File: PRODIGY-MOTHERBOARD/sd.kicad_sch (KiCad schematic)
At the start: 8 parts, among them J21 DM3BT-DSF-PEJS/C, Q1 DMP2045U-7, U4 IP4252CZ16

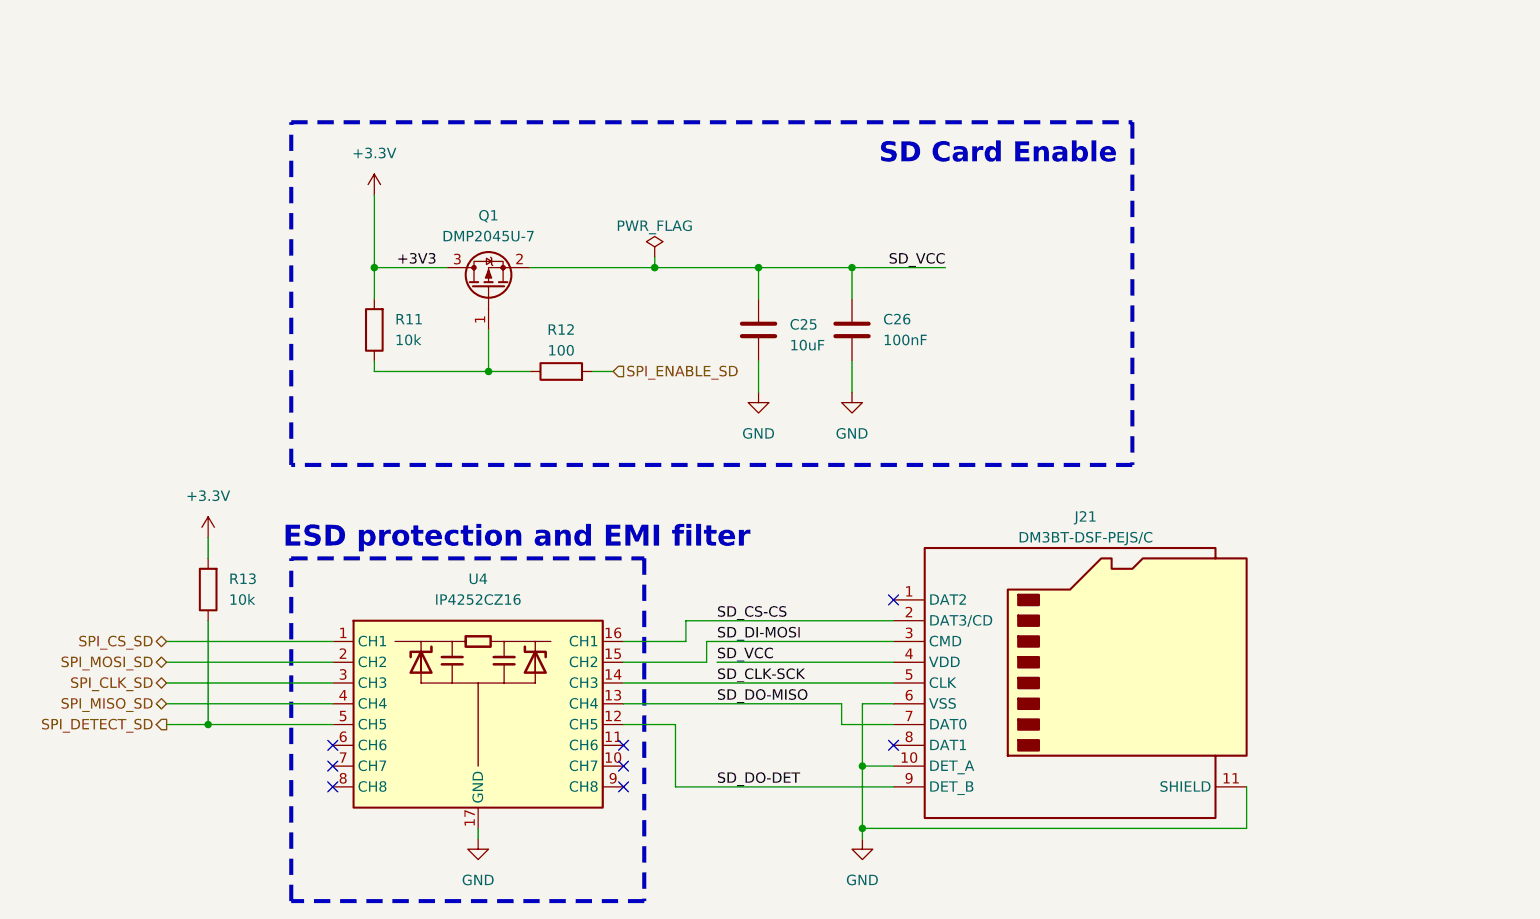
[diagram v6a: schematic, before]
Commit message: Submitted V0 for evaluation. Avaiting feedback.
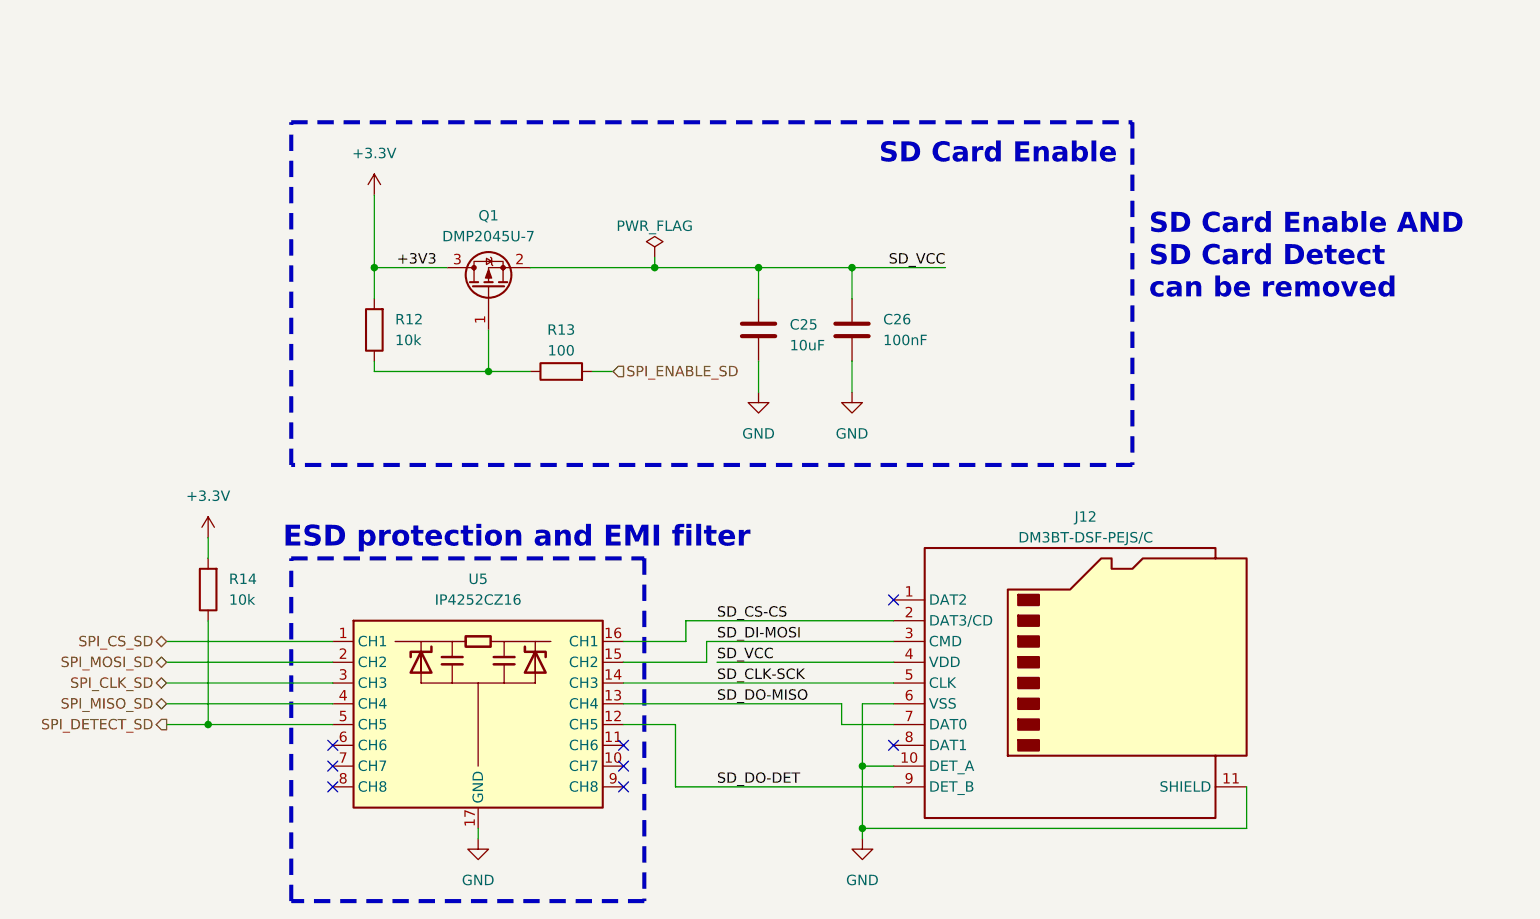
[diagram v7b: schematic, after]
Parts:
- renumbered J21 to J12, R11 to R12, R12 to R13, R13 to R14, U4 to U5
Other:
- note added: "SD Card Enable AND SD Card Detect can be removed"
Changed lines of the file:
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@@
 		)
 	)
-	(text "SD Card Enable"
-		(exclude_from_sim no)
-		(at 172.212 45.974 0)
+	(text "SD Card Enable AND\nSD Card Detect\ncan be removed"
+		(exclude_from_sim no)
+		(at 205.232 62.484 0)
 		(effects
 			(font
@@
 		)
 	)
+	(text "SD Card Enable"
+		(exclude_from_sim no)
+		(at 172.212 45.974 0)
+		(effects
+			(font
+				(size 2.45 2.45)
+				(thickness 0.49)
+				(bold yes)
+			)
+			(justify left bottom)
+		)
+	)
 	(label "SD_DI-MOSI"
 		(at 152.4 104.14 0)
@@
 		(dnp no)
 		(fields_autoplaced yes)
-		(property "Reference" "#PWR040"
+		(property "Reference" "#PWR064"
 			(at 123.19 134.62 0)
 			(effects
@@
 			(project "PRODIGY-MOTHERBOARD"
 				(path "/f1c25860-8989-4190-bd24-2491d23ca7d9/e2913798-f444-47a6-8b64-53020d7d816b/c4f3c4b1-d676-4f7b-883c-6fdba835d106"
-					(reference "#PWR040")
+					(reference "#PWR064")
 					(unit 1)
 				)
@@
 		(dnp no)
 		(fields_autoplaced yes)
-		(property "Reference" "R12"
+		(property "Reference" "R13"
 			(at 133.35 66.04 90)
 			(effects
@@
 			(project "PRODIGY-MOTHERBOARD"
 				(path "/f1c25860-8989-4190-bd24-2491d23ca7d9/e2913798-f444-47a6-8b64-53020d7d816b/c4f3c4b1-d676-4f7b-883c-6fdba835d106"
-					(reference "R12")
+					(reference "R13")
 					(unit 1)
 				)
@@
 		(dnp no)
 		(fields_autoplaced yes)
-		(property "Reference" "R11"
+		(property "Reference" "R12"
 			(at 113.03 64.7699 0)
 			(effects
@@
 			(project "PRODIGY-MOTHERBOARD"
 				(path "/f1c25860-8989-4190-bd24-2491d23ca7d9/e2913798-f444-47a6-8b64-53020d7d816b/c4f3c4b1-d676-4f7b-883c-6fdba835d106"
-					(reference "R11")
+					(reference "R12")
 					(unit 1)
 				)
@@
 		(dnp no)
 		(fields_autoplaced yes)
-		(property "Reference" "#PWR036"
+		(property "Reference" "#PWR060"
 			(at 110.49 53.34 0)
 			(effects
@@
 			(project "PRODIGY-MOTHERBOARD"
 				(path "/f1c25860-8989-4190-bd24-2491d23ca7d9/e2913798-f444-47a6-8b64-53020d7d816b/c4f3c4b1-d676-4f7b-883c-6fdba835d106"
-					(reference "#PWR036")
+					(reference "#PWR060")
 					(unit 1)
 				)
@@
 		(dnp no)
 		(fields_autoplaced yes)
-		(property "Reference" "#PWR039"
+		(property "Reference" "#PWR063"
 			(at 90.17 95.25 0)
 			(effects
@@
 			(project "PRODIGY-MOTHERBOARD"
 				(path "/f1c25860-8989-4190-bd24-2491d23ca7d9/e2913798-f444-47a6-8b64-53020d7d816b/c4f3c4b1-d676-4f7b-883c-6fdba835d106"
-					(reference "#PWR039")
+					(reference "#PWR063")
 					(unit 1)
 				)
@@
 		(dnp no)
 		(fields_autoplaced yes)
-		(property "Reference" "#PWR038"
+		(property "Reference" "#PWR062"
 			(at 168.91 80.01 0)
 			(effects
@@
 			(project "PRODIGY-MOTHERBOARD"
 				(path "/f1c25860-8989-4190-bd24-2491d23ca7d9/e2913798-f444-47a6-8b64-53020d7d816b/c4f3c4b1-d676-4f7b-883c-6fdba835d106"
-					(reference "#PWR038")
+					(reference "#PWR062")
 					(unit 1)
 				)
@@
 		(dnp no)
 		(fields_autoplaced yes)
-		(property "Reference" "#PWR041"
+		(property "Reference" "#PWR065"
 			(at 170.18 134.62 0)
 			(effects
@@
 			(project "PRODIGY-MOTHERBOARD"
 				(path "/f1c25860-8989-4190-bd24-2491d23ca7d9/e2913798-f444-47a6-8b64-53020d7d816b/c4f3c4b1-d676-4f7b-883c-6fdba835d106"
-					(reference "#PWR041")
+					(reference "#PWR065")
 					(unit 1)
 				)
@@
 		(dnp no)
 		(fields_autoplaced yes)
-		(property "Reference" "#PWR037"
+		(property "Reference" "#PWR061"
 			(at 157.48 80.01 0)
 			(effects
@@
 			(project "PRODIGY-MOTHERBOARD"
 				(path "/f1c25860-8989-4190-bd24-2491d23ca7d9/e2913798-f444-47a6-8b64-53020d7d816b/c4f3c4b1-d676-4f7b-883c-6fdba835d106"
-					(reference "#PWR037")
+					(reference "#PWR061")
 					(unit 1)
 				)
@@
 		(dnp no)
 		(fields_autoplaced yes)
-		(property "Reference" "R13"
+		(property "Reference" "R14"
 			(at 92.71 96.5199 0)
 			(effects
@@
 			(project "PRODIGY-MOTHERBOARD"
 				(path "/f1c25860-8989-4190-bd24-2491d23ca7d9/e2913798-f444-47a6-8b64-53020d7d816b/c4f3c4b1-d676-4f7b-883c-6fdba835d106"
-					(reference "R13")
+					(reference "R14")
 					(unit 1)
 				)
@@
 		(on_board yes)
 		(dnp no)
-		(property "Reference" "J21"
+		(property "Reference" "J12"
 			(at 197.485 88.9 0)
 			(effects
@@
 			(project "PRODIGY-MOTHERBOARD"
 				(path "/f1c25860-8989-4190-bd24-2491d23ca7d9/e2913798-f444-47a6-8b64-53020d7d816b/c4f3c4b1-d676-4f7b-883c-6fdba835d106"
-					(reference "J21")
+					(reference "J12")
 					(unit 1)
 				)
@@
 		(dnp no)
 		(fields_autoplaced yes)
-		(property "Reference" "U4"
+		(property "Reference" "U5"
 			(at 123.19 96.52 0)
 			(effects
@@
 			(project "PRODIGY-MOTHERBOARD"
 				(path "/f1c25860-8989-4190-bd24-2491d23ca7d9/e2913798-f444-47a6-8b64-53020d7d816b/c4f3c4b1-d676-4f7b-883c-6fdba835d106"
-					(reference "U4")
-					(unit 1)
-				)
+					(reference "U5")
+					(unit 1)
+				)

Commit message: Finished v0.1 schematic.
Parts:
- renumbered C25 to C65, C26 to C66, J12 to J21, Q1 to Q2, R14 to R38, R12 to R39, R13 to R40, U5 to U17
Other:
- note removed: "SD Card Enable AND SD Card Detect can be removed"
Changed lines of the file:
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@@
 		)
 	)
-	(text "SD Card Enable AND\nSD Card Detect\ncan be removed"
-		(exclude_from_sim no)
-		(at 205.232 62.484 0)
+	(text "SD Card Enable"
+		(exclude_from_sim no)
+		(at 172.212 45.974 0)
 		(effects
 			(font
@@
 		)
 	)
-	(text "SD Card Enable"
-		(exclude_from_sim no)
-		(at 172.212 45.974 0)
-		(effects
-			(font
-				(size 2.45 2.45)
-				(thickness 0.49)
-				(bold yes)
-			)
-			(justify left bottom)
-		)
-	)
 	(label "SD_DI-MOSI"
 		(at 152.4 104.14 0)
@@
 		(dnp no)
 		(fields_autoplaced yes)
-		(property "Reference" "#PWR064"
+		(property "Reference" "#PWR0162"
 			(at 123.19 134.62 0)
 			(effects
@@
 			(project "PRODIGY-MOTHERBOARD"
 				(path "/f1c25860-8989-4190-bd24-2491d23ca7d9/e2913798-f444-47a6-8b64-53020d7d816b/c4f3c4b1-d676-4f7b-883c-6fdba835d106"
-					(reference "#PWR064")
+					(reference "#PWR0162")
 					(unit 1)
 				)
@@
 		(dnp no)
 		(fields_autoplaced yes)
-		(property "Reference" "R13"
+		(property "Reference" "R40"
 			(at 133.35 66.04 90)
 			(effects
@@
 			(project "PRODIGY-MOTHERBOARD"
 				(path "/f1c25860-8989-4190-bd24-2491d23ca7d9/e2913798-f444-47a6-8b64-53020d7d816b/c4f3c4b1-d676-4f7b-883c-6fdba835d106"
-					(reference "R13")
+					(reference "R40")
 					(unit 1)
 				)
@@
 		(dnp no)
 		(fields_autoplaced yes)
-		(property "Reference" "R12"
+		(property "Reference" "R39"
 			(at 113.03 64.7699 0)
 			(effects
@@
 			(project "PRODIGY-MOTHERBOARD"
 				(path "/f1c25860-8989-4190-bd24-2491d23ca7d9/e2913798-f444-47a6-8b64-53020d7d816b/c4f3c4b1-d676-4f7b-883c-6fdba835d106"
-					(reference "R12")
+					(reference "R39")
 					(unit 1)
 				)
@@
 		(dnp no)
 		(fields_autoplaced yes)
-		(property "Reference" "#PWR060"
+		(property "Reference" "#PWR0161"
 			(at 110.49 53.34 0)
 			(effects
@@
 			(project "PRODIGY-MOTHERBOARD"
 				(path "/f1c25860-8989-4190-bd24-2491d23ca7d9/e2913798-f444-47a6-8b64-53020d7d816b/c4f3c4b1-d676-4f7b-883c-6fdba835d106"
-					(reference "#PWR060")
+					(reference "#PWR0161")
 					(unit 1)
 				)
@@
 		(dnp no)
 		(fields_autoplaced yes)
-		(property "Reference" "#PWR063"
+		(property "Reference" "#PWR0160"
 			(at 90.17 95.25 0)
 			(effects
@@
 			(project "PRODIGY-MOTHERBOARD"
 				(path "/f1c25860-8989-4190-bd24-2491d23ca7d9/e2913798-f444-47a6-8b64-53020d7d816b/c4f3c4b1-d676-4f7b-883c-6fdba835d106"
-					(reference "#PWR063")
+					(reference "#PWR0160")
 					(unit 1)
 				)
@@
 		(dnp no)
 		(fields_autoplaced yes)
-		(property "Reference" "Q1"
+		(property "Reference" "Q2"
 			(at 124.46 52.07 90)
 			(effects
@@
 			(project "PRODIGY-MOTHERBOARD"
 				(path "/f1c25860-8989-4190-bd24-2491d23ca7d9/e2913798-f444-47a6-8b64-53020d7d816b/c4f3c4b1-d676-4f7b-883c-6fdba835d106"
-					(reference "Q1")
+					(reference "Q2")
 					(unit 1)
 				)
@@
 		(dnp no)
 		(fields_autoplaced yes)
-		(property "Reference" "#PWR062"
+		(property "Reference" "#PWR0164"
 			(at 168.91 80.01 0)
 			(effects
@@
 			(project "PRODIGY-MOTHERBOARD"
 				(path "/f1c25860-8989-4190-bd24-2491d23ca7d9/e2913798-f444-47a6-8b64-53020d7d816b/c4f3c4b1-d676-4f7b-883c-6fdba835d106"
-					(reference "#PWR062")
+					(reference "#PWR0164")
 					(unit 1)
 				)
@@
 		(dnp no)
 		(fields_autoplaced yes)
-		(property "Reference" "#PWR065"
+		(property "Reference" "#PWR0165"
 			(at 170.18 134.62 0)
 			(effects
@@
 			(project "PRODIGY-MOTHERBOARD"
 				(path "/f1c25860-8989-4190-bd24-2491d23ca7d9/e2913798-f444-47a6-8b64-53020d7d816b/c4f3c4b1-d676-4f7b-883c-6fdba835d106"
-					(reference "#PWR065")
+					(reference "#PWR0165")
 					(unit 1)
 				)
@@
 		(dnp no)
 		(fields_autoplaced yes)
-		(property "Reference" "C25"
+		(property "Reference" "C65"
 			(at 161.29 65.405 0)
 			(effects
@@
 			(project "PRODIGY-MOTHERBOARD"
 				(path "/f1c25860-8989-4190-bd24-2491d23ca7d9/e2913798-f444-47a6-8b64-53020d7d816b/c4f3c4b1-d676-4f7b-883c-6fdba835d106"
-					(reference "C25")
+					(reference "C65")
 					(unit 1)
 				)
@@
 		(dnp no)
 		(fields_autoplaced yes)
-		(property "Reference" "#PWR061"
+		(property "Reference" "#PWR0163"
 			(at 157.48 80.01 0)
 			(effects
@@
 			(project "PRODIGY-MOTHERBOARD"
 				(path "/f1c25860-8989-4190-bd24-2491d23ca7d9/e2913798-f444-47a6-8b64-53020d7d816b/c4f3c4b1-d676-4f7b-883c-6fdba835d106"
-					(reference "#PWR061")
+					(reference "#PWR0163")
 					(unit 1)
 				)
@@
 		(dnp no)
 		(fields_autoplaced yes)
-		(property "Reference" "R14"
+		(property "Reference" "R38"
 			(at 92.71 96.5199 0)
 			(effects
@@
 			(project "PRODIGY-MOTHERBOARD"
 				(path "/f1c25860-8989-4190-bd24-2491d23ca7d9/e2913798-f444-47a6-8b64-53020d7d816b/c4f3c4b1-d676-4f7b-883c-6fdba835d106"
-					(reference "R14")
+					(reference "R38")
 					(unit 1)
 				)
@@
 		(dnp no)
 		(fields_autoplaced yes)
-		(property "Reference" "C26"
+		(property "Reference" "C66"
 			(at 172.72 64.7699 0)
 			(effects
@@
 			(project "PRODIGY-MOTHERBOARD"
 				(path "/f1c25860-8989-4190-bd24-2491d23ca7d9/e2913798-f444-47a6-8b64-53020d7d816b/c4f3c4b1-d676-4f7b-883c-6fdba835d106"
-					(reference "C26")
+					(reference "C66")
 					(unit 1)
 				)
@@
 		(on_board yes)
 		(dnp no)
-		(property "Reference" "J12"
+		(property "Reference" "J21"
 			(at 197.485 88.9 0)
 			(effects
@@
 			(project "PRODIGY-MOTHERBOARD"
 				(path "/f1c25860-8989-4190-bd24-2491d23ca7d9/e2913798-f444-47a6-8b64-53020d7d816b/c4f3c4b1-d676-4f7b-883c-6fdba835d106"
-					(reference "J12")
+					(reference "J21")
 					(unit 1)
 				)
@@
 		(dnp no)
 		(fields_autoplaced yes)
-		(property "Reference" "U5"
+		(property "Reference" "U17"
 			(at 123.19 96.52 0)
 			(effects
@@
 			(project "PRODIGY-MOTHERBOARD"
 				(path "/f1c25860-8989-4190-bd24-2491d23ca7d9/e2913798-f444-47a6-8b64-53020d7d816b/c4f3c4b1-d676-4f7b-883c-6fdba835d106"
-					(reference "U5")
-					(unit 1)
-				)
+					(reference "U17")
+					(unit 1)
+				)
